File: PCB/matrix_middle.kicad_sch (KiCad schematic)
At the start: 62 parts, among them J10 Conn_02x02_Top_Bottom, J12 Conn_02x02_Top_Bottom, J14 Conn_02x02_Top_Bottom, J15 Conn_02x02_Top_Bottom, J16 Conn_02x02_Top_Bottom, J17 Conn_02x02_Top_Bottom, J18 Conn_02x02_Top_Bottom, J19 Conn_02x02_Top_Bottom, J20 Conn_02x02_Top_Bottom, J25 Conn_02x02_Top_Bottom, J26 Conn_02x02_Top_Bottom, J9 Conn_02x02_Top_Bottom

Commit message: キースイッチを配置
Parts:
- J10, J12, J14, J15, J16, J17, J18, J19, J20, J25, J26, J9: footprint Connector_PinHeader_2.54mm:PinHeader_2x02_P2.54mm_Vertical -> Connector_PinHeader_2.00mm:PinHeader_2x02_P2.00mm_Vertical
- SW_TAB1.25u1: footprint MX_Alps_Hybrid:MXOnly-1.5U-Hotswap-guide -> MX_Alps_Hybrid:MXOnly-1.25U-NoLED
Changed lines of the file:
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@@
     (property "Reference" "J17" (id 0) (at 85.09 216.0102 0))
     (property "Value" "Conn_02x02_Top_Bottom" (id 1) (at 85.09 218.5471 0))
-    (property "Footprint" "Connector_PinHeader_2.54mm:PinHeader_2x02_P2.54mm_Vertical" (id 2) (at 83.82 220.98 0)
+    (property "Footprint" "Connector_PinHeader_2.00mm:PinHeader_2x02_P2.00mm_Vertical" (id 2) (at 83.82 220.98 0)
       (effects (font (size 1.27 1.27)) hide)
     )
@@
     (property "Reference" "J12" (id 0) (at 123.19 180.4502 0))
     (property "Value" "Conn_02x02_Top_Bottom" (id 1) (at 123.19 182.9871 0))
-    (property "Footprint" "Connector_PinHeader_2.54mm:PinHeader_2x02_P2.54mm_Vertical" (id 2) (at 121.92 185.42 0)
+    (property "Footprint" "Connector_PinHeader_2.00mm:PinHeader_2x02_P2.00mm_Vertical" (id 2) (at 121.92 185.42 0)
       (effects (font (size 1.27 1.27)) hide)
     )
@@
     (property "Reference" "J18" (id 0) (at 123.19 195.6902 0))
     (property "Value" "Conn_02x02_Top_Bottom" (id 1) (at 123.19 198.2271 0))
-    (property "Footprint" "Connector_PinHeader_2.54mm:PinHeader_2x02_P2.54mm_Vertical" (id 2) (at 121.92 200.66 0)
+    (property "Footprint" "Connector_PinHeader_2.00mm:PinHeader_2x02_P2.00mm_Vertical" (id 2) (at 121.92 200.66 0)
       (effects (font (size 1.27 1.27)) hide)
     )
@@
     (property "Reference" "SW_TAB1.25u1" (id 0) (at 43.18 72.771 0))
     (property "Value" "SW_Push" (id 1) (at 43.18 75.0824 0))
-    (property "Footprint" "MX_Alps_Hybrid:MXOnly-1.5U-Hotswap-guide" (id 2) (at 43.18 74.93 0)
+    (property "Footprint" "MX_Alps_Hybrid:MXOnly-1.25U-NoLED" (id 2) (at 43.18 74.93 0)
       (effects (font (size 1.27 1.27)) hide)
     )
@@
     (property "Reference" "J26" (id 0) (at 135.89 249.0302 0))
     (property "Value" "Conn_02x02_Top_Bottom" (id 1) (at 135.89 251.5671 0))
-    (property "Footprint" "Connector_PinHeader_2.54mm:PinHeader_2x02_P2.54mm_Vertical" (id 2) (at 134.62 254 0)
+    (property "Footprint" "Connector_PinHeader_2.00mm:PinHeader_2x02_P2.00mm_Vertical" (id 2) (at 134.62 254 0)
       (effects (font (size 1.27 1.27)) hide)
     )
@@
     (property "Reference" "J14" (id 0) (at 166.37 180.4502 0))
     (property "Value" "Conn_02x02_Top_Bottom" (id 1) (at 166.37 182.9871 0))
-    (property "Footprint" "Connector_PinHeader_2.54mm:PinHeader_2x02_P2.54mm_Vertical" (id 2) (at 165.1 185.42 0)
+    (property "Footprint" "Connector_PinHeader_2.00mm:PinHeader_2x02_P2.00mm_Vertical" (id 2) (at 165.1 185.42 0)
       (effects (font (size 1.27 1.27)) hide)
     )
@@
     (property "Reference" "J25" (id 0) (at 85.09 249.0302 0))
     (property "Value" "Conn_02x02_Top_Bottom" (id 1) (at 85.09 251.5671 0))
-    (property "Footprint" "Connector_PinHeader_2.54mm:PinHeader_2x02_P2.54mm_Vertical" (id 2) (at 83.82 254 0)
+    (property "Footprint" "Connector_PinHeader_2.00mm:PinHeader_2x02_P2.00mm_Vertical" (id 2) (at 83.82 254 0)
       (effects (font (size 1.27 1.27)) hide)
     )
@@
     (property "Reference" "J20" (id 0) (at 186.69 216.0102 0))
     (property "Value" "Conn_02x02_Top_Bottom" (id 1) (at 186.69 218.5471 0))
-    (property "Footprint" "Connector_PinHeader_2.54mm:PinHeader_2x02_P2.54mm_Vertical" (id 2) (at 185.42 220.98 0)
+    (property "Footprint" "Connector_PinHeader_2.00mm:PinHeader_2x02_P2.00mm_Vertical" (id 2) (at 185.42 220.98 0)
       (effects (font (size 1.27 1.27)) hide)
     )
@@
     (property "Reference" "J10" (id 0) (at 80.01 180.4502 0))
     (property "Value" "Conn_02x02_Top_Bottom" (id 1) (at 80.01 182.9871 0))
-    (property "Footprint" "Connector_PinHeader_2.54mm:PinHeader_2x02_P2.54mm_Vertical" (id 2) (at 78.74 185.42 0)
+    (property "Footprint" "Connector_PinHeader_2.00mm:PinHeader_2x02_P2.00mm_Vertical" (id 2) (at 78.74 185.42 0)
       (effects (font (size 1.27 1.27)) hide)
     )
@@
     (property "Reference" "J15" (id 0) (at 34.29 216.0102 0))
     (property "Value" "Conn_02x02_Top_Bottom" (id 1) (at 34.29 218.5471 0))
-    (property "Footprint" "Connector_PinHeader_2.54mm:PinHeader_2x02_P2.54mm_Vertical" (id 2) (at 33.02 220.98 0)
+    (property "Footprint" "Connector_PinHeader_2.00mm:PinHeader_2x02_P2.00mm_Vertical" (id 2) (at 33.02 220.98 0)
       (effects (font (size 1.27 1.27)) hide)
     )
@@
     (property "Reference" "J16" (id 0) (at 80.01 195.6902 0))
     (property "Value" "Conn_02x02_Top_Bottom" (id 1) (at 80.01 198.2271 0))
-    (property "Footprint" "Connector_PinHeader_2.54mm:PinHeader_2x02_P2.54mm_Vertical" (id 2) (at 78.74 200.66 0)
+    (property "Footprint" "Connector_PinHeader_2.00mm:PinHeader_2x02_P2.00mm_Vertical" (id 2) (at 78.74 200.66 0)
       (effects (font (size 1.27 1.27)) hide)
     )
@@
     (property "Reference" "J9" (id 0) (at 36.83 180.4502 0))
     (property "Value" "Conn_02x02_Top_Bottom" (id 1) (at 36.83 182.9871 0))
-    (property "Footprint" "Connector_PinHeader_2.54mm:PinHeader_2x02_P2.54mm_Vertical" (id 2) (at 35.56 185.42 0)
+    (property "Footprint" "Connector_PinHeader_2.00mm:PinHeader_2x02_P2.00mm_Vertical" (id 2) (at 35.56 185.42 0)
       (effects (font (size 1.27 1.27)) hide)
     )
@@
     (property "Reference" "J19" (id 0) (at 135.89 216.0102 0))
     (property "Value" "Conn_02x02_Top_Bottom" (id 1) (at 135.89 218.5471 0))
-    (property "Footprint" "Connector_PinHeader_2.54mm:PinHeader_2x02_P2.54mm_Vertical" (id 2) (at 134.62 220.98 0)
-      (effects (font (size 1.27 1.27)) hide)
-    )
+    (property "Footprint" "Connector_PinHeader_2.00mm:PinHeader_2x02_P2.00mm_Vertical" (id 2) (at 134.62 220.98 0)
+      (effects (font (size 1.27 1.27)) hide)
+    )

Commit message: 部品仮配置
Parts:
- J11: renamed from J9; footprint Connector_PinHeader_2.00mm:PinHeader_2x02_P2.00mm_Vertical -> locallib:PinHeader_2x02_P2.00mm_Vertical_Centered
- J12: renamed from J10; footprint Connector_PinHeader_2.00mm:PinHeader_2x02_P2.00mm_Vertical -> locallib:PinHeader_2x02_P2.00mm_Vertical_Centered
- J13: renamed from J12; footprint Connector_PinHeader_2.00mm:PinHeader_2x02_P2.00mm_Vertical -> locallib:PinHeader_2x02_P2.00mm_Vertical_Centered
- J14, J19, J20: footprint Connector_PinHeader_2.00mm:PinHeader_2x02_P2.00mm_Vertical -> locallib:PinHeader_2x02_P2.00mm_Vertical_Centered
- J15: renamed from J16; footprint Connector_PinHeader_2.00mm:PinHeader_2x02_P2.00mm_Vertical -> locallib:PinHeader_2x02_P2.00mm_Vertical_Centered
- J16: renamed from J18; footprint Connector_PinHeader_2.00mm:PinHeader_2x02_P2.00mm_Vertical -> locallib:PinHeader_2x02_P2.00mm_Vertical_Centered
- J17: renamed from J15; footprint Connector_PinHeader_2.00mm:PinHeader_2x02_P2.00mm_Vertical -> locallib:PinHeader_2x02_P2.00mm_Vertical_Centered
- J18: renamed from J17; footprint Connector_PinHeader_2.00mm:PinHeader_2x02_P2.00mm_Vertical -> locallib:PinHeader_2x02_P2.00mm_Vertical_Centered
- J21: renamed from J25; footprint Connector_PinHeader_2.00mm:PinHeader_2x02_P2.00mm_Vertical -> locallib:PinHeader_2x02_P2.00mm_Vertical_Centered
- J22: renamed from J26; footprint Connector_PinHeader_2.00mm:PinHeader_2x02_P2.00mm_Vertical -> locallib:PinHeader_2x02_P2.00mm_Vertical_Centered
- renumbered EXT_C8 to EXT_MC0, EXT_C9 to EXT_MC1, EXT_C10 to EXT_MC2, EXT_C11 to EXT_MC3, EXT_C12 to EXT_MC4, EXT_C13 to EXT_MC5, EXT_C14 to EXT_MC6, EXT_C15 to EXT_MC7, EXT_R10 to EXT_MR0, EXT_R12 to EXT_MR1, EXT_R14 to EXT_MR2, EXT_R16 to EXT_MR3, EXT_R11 to EXT_MR5, EXT_R13 to EXT_MR6, EXT_R15 to EXT_MR7, EXT_R17 to EXT_MR8

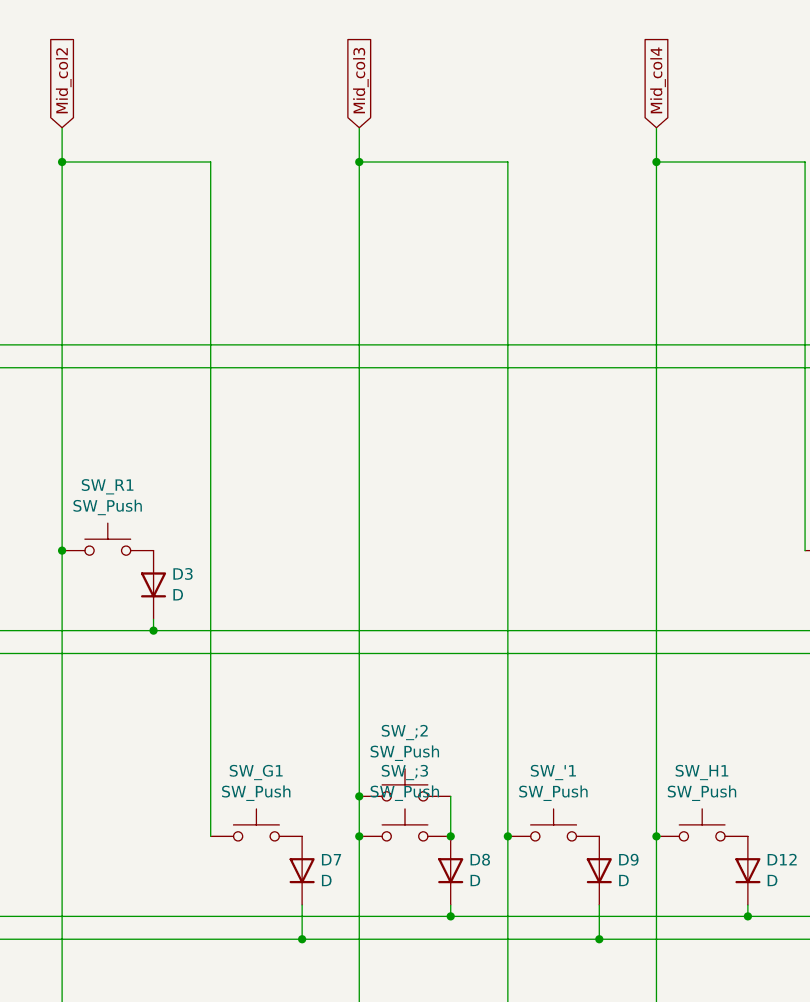
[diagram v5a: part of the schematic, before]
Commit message: スイッチ方向確定。細かな調整
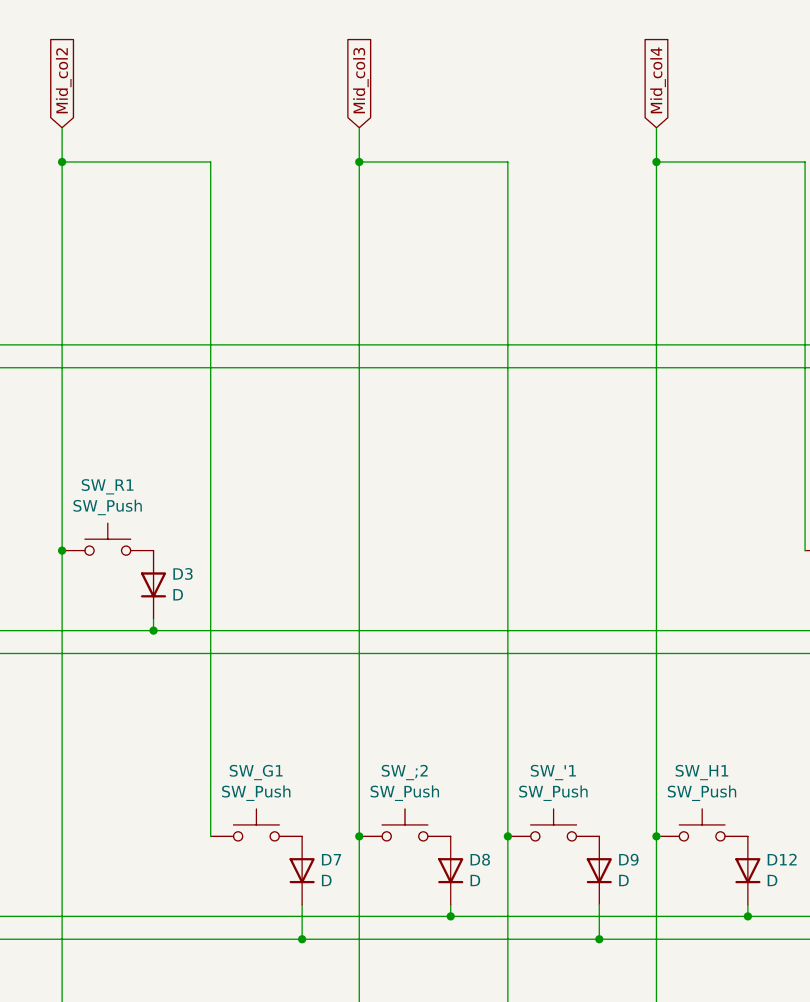
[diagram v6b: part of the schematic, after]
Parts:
- removed SW_;3: SW_Push, MX_Alps_Hybrid:MXOnly-1U-NoLED, symbol Switch:SW_Push
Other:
- moved on the sheet: SW_;2
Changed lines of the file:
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@@
   (junction (at 48.26 93.98) (diameter 0) (color 0 0 0 0)
   )
+  (junction (at 137.16 116.84) (diameter 0) (color 0 0 0 0)
+  )
   (junction (at 43.18 220.98) (diameter 0) (color 0 0 0 0)
   )
@@
   (junction (at 177.8 220.98) (diameter 0) (color 0 0 0 0)
   )
-  (junction (at 137.16 112.395) (diameter 0) (color 0 0 0 0)
-  )
   (junction (at 236.22 85.09) (diameter 0) (color 0 0 0 0)
   )
   (junction (at 195.58 223.52) (diameter 0) (color 0 0 0 0)
   )
-  (junction (at 137.16 116.84) (diameter 0) (color 0 0 0 0)
-  )
   (junction (at 147.32 125.73) (diameter 0) (color 0 0 0 0)
   )
@@
   (junction (at 203.2 41.91) (diameter 0) (color 0 0 0 0)
   )
-  (junction (at 147.32 116.84) (diameter 0) (color 0 0 0 0)
-  )
   (junction (at 64.77 96.52) (diameter 0) (color 0 0 0 0)
   )
@@
     (stroke (width 0) (type default) (color 0 0 0 0))
   )
+  (wire (pts (xy 137.16 116.84) (xy 137.16 148.59))
+    (stroke (width 0) (type default) (color 0 0 0 0))
+  )
   (wire (pts (xy 64.77 96.52) (xy 196.85 96.52))
     (stroke (width 0) (type default) (color 0 0 0 0))
@@
     (stroke (width 0) (type default) (color 0 0 0 0))
   )
-  (wire (pts (xy 137.16 116.84) (xy 137.16 148.59))
-    (stroke (width 0) (type default) (color 0 0 0 0))
-  )
   (wire (pts (xy 170.18 38.1) (xy 170.18 41.91))
     (stroke (width 0) (type default) (color 0 0 0 0))
@@
     (stroke (width 0) (type default) (color 0 0 0 0))
   )
-  (wire (pts (xy 147.32 112.395) (xy 147.32 116.84))
-    (stroke (width 0) (type default) (color 0 0 0 0))
-  )
   (wire (pts (xy 163.83 128.27) (xy 279.4 128.27))
     (stroke (width 0) (type default) (color 0 0 0 0))
@@
     (stroke (width 0) (type default) (color 0 0 0 0))
   )
-  (wire (pts (xy 137.16 41.91) (xy 137.16 112.395))
+  (wire (pts (xy 137.16 41.91) (xy 137.16 116.84))
     (stroke (width 0) (type default) (color 0 0 0 0))
   )
@@
   )
   (wire (pts (xy 180.34 157.48) (xy 279.4 157.48))
-    (stroke (width 0) (type default) (color 0 0 0 0))
-  )
-  (wire (pts (xy 137.16 112.395) (xy 137.16 116.84))
     (stroke (width 0) (type default) (color 0 0 0 0))
   )
@@
     (pin "2")
   )
-  (symbol (lib_id "Switch:SW_Push") (at 142.24 116.84 0) (unit 1)
-    (in_bom yes) (on_board yes)
-    (property "Reference" "SW_;3" (id 0) (at 142.24 109.601 0))
-    (property "Value" "SW_Push" (id 1) (at 142.24 111.9124 0))
-    (property "Footprint" "MX_Alps_Hybrid:MXOnly-1U-NoLED" (id 2) (at 142.24 111.76 0)
-      (effects (font (size 1.27 1.27)) hide)
-    )
-    (property "Datasheet" "~" (id 3) (at 142.24 111.76 0)
-      (effects (font (size 1.27 1.27)) hide)
-    )
-    (pin "1")
-    (pin "2")
-  )
   (symbol (lib_id "Device:D") (at 48.26 88.9 90) (unit 1)
     (in_bom yes) (on_board yes)
@@
     (pin "1")
   )
-  (symbol (lib_id "Switch:SW_Push") (at 142.24 112.395 0) (unit 1)
-    (in_bom yes) (on_board yes)
-    (property "Reference" "SW_;2" (id 0) (at 142.24 105.156 0))
-    (property "Value" "SW_Push" (id 1) (at 142.24 107.4674 0))
-    (property "Footprint" "MX_Alps_Hybrid:MXOnly-1U-Hotswap-guide" (id 2) (at 142.24 107.315 0)
-      (effects (font (size 1.27 1.27)) hide)
-    )
-    (property "Datasheet" "~" (id 3) (at 142.24 107.315 0)
-      (effects (font (size 1.27 1.27)) hide)
-    )
+  (symbol (lib_id "Switch:SW_Push") (at 142.24 116.84 0) (unit 1)
+    (in_bom yes) (on_board yes)
+    (property "Reference" "SW_;2" (id 0) (at 142.24 109.601 0))
+    (property "Value" "SW_Push" (id 1) (at 142.24 111.9124 0))
+    (property "Footprint" "MX_Alps_Hybrid:MXOnly-1U-Hotswap-guide" (id 2) (at 142.24 111.76 0)
+      (effects (font (size 1.27 1.27)) hide)
+    )
+    (property "Datasheet" "~" (id 3) (at 142.24 111.76 0)
+      (effects (font (size 1.27 1.27)) hide)
+    )

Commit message: 5wayスイッチを追加するテスト
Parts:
- added S?: JS5208, SW_JS5208, symbol JS5208:JS5208
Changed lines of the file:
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@@
+      )
+    )
+    (symbol "JS5208:JS5208" (pin_names (offset 1.016)) (in_bom yes) (on_board yes)
+      (property "Reference" "S" (id 0) (at -5.08 6.35 0)
+        (effects (font (size 1.27 1.27)) (justify left bottom))
+      )
+      (property "Value" "JS5208" (id 1) (at -5.08 -7.62 0)
+        (effects (font (size 1.27 1.27)) (justify left bottom))
+      )
+      (property "Footprint" "SW_JS5208" (id 2) (at 0 0 0)
+        (effects (font (size 1.27 1.27)) (justify bottom) hide)
+      )
+      (property "Datasheet" "" (id 3) (at 0 0 0)
+        (effects (font (size 1.27 1.27)) hide)
+      )
+      (property "STANDARD" "Manufacturer Recommendations" (id 4) (at 0 0 0)
+        (effects (font (size 1.27 1.27)) (justify bottom) hide)
+      )
+      (property "MAXIMUM_PACKAGE_HEIGHT" "12.6 mm" (id 5) (at 0 0 0)
+        (effects (font (size 1.27 1.27)) (justify bottom) hide)
+      )
+      (property "PARTREV" "D" (id 6) (at 0 0 0)
+        (effects (font (size 1.27 1.27)) (justify bottom) hide)
+      )
+      (property "MANUFACTURER" "E-Switch" (id 7) (at 0 0 0)
+        (effects (font (size 1.27 1.27)) (justify bottom) hide)
+      )
+      (symbol "JS5208_0_0"
+        (rectangle (start -5.08 -5.08) (end 5.08 5.08)
+          (stroke (width 0.254) (type default) (color 0 0 0 0))
+          (fill (type background))
+        )
+        (circle (center -2.54 0) (radius 0.3302)
+          (stroke (width 0.1524) (type default) (color 0 0 0 0))
+          (fill (type none))
+        )
+        (circle (center 0 -2.54) (radius 0.3302)
+          (stroke (width 0.1524) (type default) (color 0 0 0 0))
+          (fill (type none))
+        )
+        (polyline
+          (pts
+            (xy -5.08 -2.54)
+            (xy -3.81 -2.54)
+          )
+          (stroke (width 0.1524) (type default) (color 0 0 0 0))
+          (fill (type none))
+        )
+        (polyline
+          (pts
+            (xy -5.08 0)
+            (xy -2.921 0)
+          )
+          (stroke (width 0.1524) (type default) (color 0 0 0 0))
+          (fill (type none))
+        )
+        (polyline
+          (pts
+            (xy -5.08 2.54)
+            (xy -2.54 2.54)
+          )
+          (stroke (width 0.1524) (type default) (color 0 0 0 0))
+          (fill (type none))
+        )
+        (polyline
+          (pts
+            (xy -3.81 -2.54)
+            (xy -3.81 -3.81)
+          )
+          (stroke (width 0.1524) (type default) (color 0 0 0 0))
+          (fill (type none))
+        )
+        (polyline
+          (pts
+            (xy -2.54 2.54)
+            (xy -0.254 0.254)
+          )
+          (stroke (width 0.1524) (type default) (color 0 0 0 0))
+          (fill (type none))
+        )
+        (polyline
+          (pts
+            (xy 0.254 -0.254)
+            (xy 1.905 -1.905)
+          )
+          (stroke (width 0.1524) (type default) (color 0 0 0 0))
+          (fill (type none))
+        )
+        (polyline
+          (pts
+            (xy 0.381 -2.54)
+            (xy 5.08 -2.54)
+          )
+          (stroke (width 0.1524) (type default) (color 0 0 0 0))
+          (fill (type none))
+        )
+        (polyline
+          (pts
+            (xy 0.381 2.54)
+            (xy 5.08 2.54)
+          )
+          (stroke (width 0.1524) (type default) (color 0 0 0 0))
+          (fill (type none))
+        )
+        (polyline
+          (pts
+            (xy 2.921 0)
+            (xy 5.08 0)
+          )
+          (stroke (width 0.1524) (type default) (color 0 0 0 0))
+          (fill (type none))
+        )
+        (circle (center 0 0) (radius 0.3302)
+          (stroke (width 0.1524) (type default) (color 0 0 0 0))
+          (fill (type none))
+        )
+        (circle (center 0 2.54) (radius 0.3302)
+          (stroke (width 0.1524) (type default) (color 0 0 0 0))
+          (fill (type none))
+        )
+        (circle (center 2.54 0) (radius 0.3302)
+          (stroke (width 0.1524) (type default) (color 0 0 0 0))
+          (fill (type none))
+        )
+        (pin passive line (at -10.16 2.54 0) (length 5.08)
+          (name "~" (effects (font (size 1.016 1.016))))
+          (number "1" (effects (font (size 1.016 1.016))))
+        )
+        (pin passive line (at -10.16 0 0) (length 5.08)
+          (name "~" (effects (font (size 1.016 1.016))))
+          (number "2" (effects (font (size 1.016 1.016))))
+        )
+        (pin passive line (at -10.16 -2.54 0) (length 5.08)
+          (name "~" (effects (font (size 1.016 1.016))))
+          (number "3" (effects (font (size 1.016 1.016))))
+        )
+        (pin passive line (at 10.16 2.54 180) (length 5.08)
+          (name "~" (effects (font (size 1.016 1.016))))
+          (number "4" (effects (font (size 1.016 1.016))))
+        )
+        (pin passive line (at 10.16 0 180) (length 5.08)
+          (name "~" (effects (font (size 1.016 1.016))))
+          (number "5" (effects (font (size 1.016 1.016))))
+        )
+        (pin passive line (at 10.16 -2.54 180) (length 5.08)
+          (name "~" (effects (font (size 1.016 1.016))))
+          (number "6" (effects (font (size 1.016 1.016))))
+        )
       )
     )
@@
     (pin "4")
   )
+  (symbol (lib_id "JS5208:JS5208") (at 205.74 186.69 0) (unit 1)
+    (in_bom yes) (on_board yes) (fields_autoplaced)
+    (property "Reference" "S?" (id 0) (at 205.74 177.9102 0))
+    (property "Value" "JS5208" (id 1) (at 205.74 180.4471 0))
+    (property "Footprint" "SW_JS5208" (id 2) (at 205.74 186.69 0)
+      (effects (font (size 1.27 1.27)) (justify bottom) hide)
+    )
+    (property "Datasheet" "" (id 3) (at 205.74 186.69 0)
+      (effects (font (size 1.27 1.27)) hide)
+    )
+    (property "STANDARD" "Manufacturer Recommendations" (id 4) (at 205.74 186.69 0)
+      (effects (font (size 1.27 1.27)) (justify bottom) hide)
+    )
+    (property "MAXIMUM_PACKAGE_HEIGHT" "12.6 mm" (id 5) (at 205.74 186.69 0)
+      (effects (font (size 1.27 1.27)) (justify bottom) hide)
+    )
+    (property "PARTREV" "D" (id 6) (at 205.74 186.69 0)
+      (effects (font (size 1.27 1.27)) (justify bottom) hide)
+    )
+    (property "MANUFACTURER" "E-Switch" (id 7) (at 205.74 186.69 0)
+      (effects (font (size 1.27 1.27)) (justify bottom) hide)
+    )
+    (pin "1")
+    (pin "2")
+    (pin "3")
+    (pin "4")
+    (pin "5")
+    (pin "6")
+  )
   (symbol (lib_id "Switch:SW_Push") (at 241.3 85.09 0) (unit 1)

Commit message: JSTコネクタとスペーサーでなんとするテスト
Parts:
- added D60, D61, D62, D63, D64: D, Diode_SMD:D_SOD-123, symbol Device:D
- added S2: JS5208, locallib:SW_JS5208_add_MP_hole, symbol JS5208:JS5208
- S1: renamed from S?; footprint SW_JS5208 -> locallib:SW_JS5208_add_MP_hole
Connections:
- net Mid_col7: now also S1.1, S2.1
- net Mid_row1: now also D60.1 (K)
- net Mid_row2: now also D61.1 (K)
- net Mid_row6: now also D64.1 (K)
- net Mid_row7: now also D62.1 (K)
- net Mid_row8: now also D63.1 (K)
- net at S1.2: now also D61.2 (A), S2.2
- net at S1.3: now also D63.2 (A), S2.3
- net at S1.4: now also D60.2 (A), S2.4
- net at S1.5: now also D62.2 (A), S2.5
- net at S1.6: now also D64.2 (A), S2.6
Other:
- note added: "5-way navigation switch"
- note added: "Bottom to Mid: require 16 pins Mid to Top: require 12 pins"
- moved on the sheet: S1
